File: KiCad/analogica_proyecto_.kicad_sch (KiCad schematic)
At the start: 0 parts

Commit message: afegit part analogica
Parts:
- added C1, C2: 1n, symbol Device:C
- added M1, M2: Conn_01x02_Pin, symbol Connector:Conn_01x02_Pin
- added U1: L298N, Package_TO_SOT_THT:TO-220-15_P2.54x5.08mm_StaggerOdd_Lead4.58mm_Vertical, symbol Driver_Motor:L298N
- added U2, U3: ACS714xLCTR-50A, Package_SO:SOIC-8_3.9x4.9mm_P1.27mm, symbol Sensor_Current:ACS714xLCTR-50A
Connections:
- new net: C1.1, U2.6 (FILTER)
- new net: C2.1, U3.6 (FILTER)
- new net AVSS: U2.8 (VCC), U3.8 (VCC)
- new net GND: C1.2, C2.2, U1.1 (SENSE_A), U1.15 (SENSE_B), U1.8 (GND), U2.5 (GND), U3.5 (GND)
- new net INA1_M1: U1.5 (IN1)
- new net INA2_M1: U1.7 (IN2)
- new net INB1_M2: U1.10 (IN3)
- new net INB2_M2: U1.12 (IN4)
- new net M1_OUT1: U1.2 (OUT1), U2.1 (IP+), U2.2 (IP+)
- new net M1_OUT2: M1.2 (Pin_2), U1.3 (OUT2)
- new net M1_OUTSEN: M1.1 (Pin_1), U2.3 (IP-), U2.4 (IP-)
- new net M2_OUT1: U1.13 (OUT3), U3.1 (IP+), U3.2 (IP+)
- new net M2_OUT2: M2.2 (Pin_2), U1.14 (OUT4)
- new net M2_OUTSEN: M2.1 (Pin_1), U3.3 (IP-), U3.4 (IP-)
- new net PWM_M1: U1.6 (EnA), U2.7 (VIOUT)
- new net PWM_M2: U1.11 (EnB), U3.7 (VIOUT)
- new net Vbat: U1.4 (Vs)
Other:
- note added: "ETAPA ANÀLOGICA"
- note added: "PONT en H"
- note added: "Pins motor"
- note added: "Sensor"

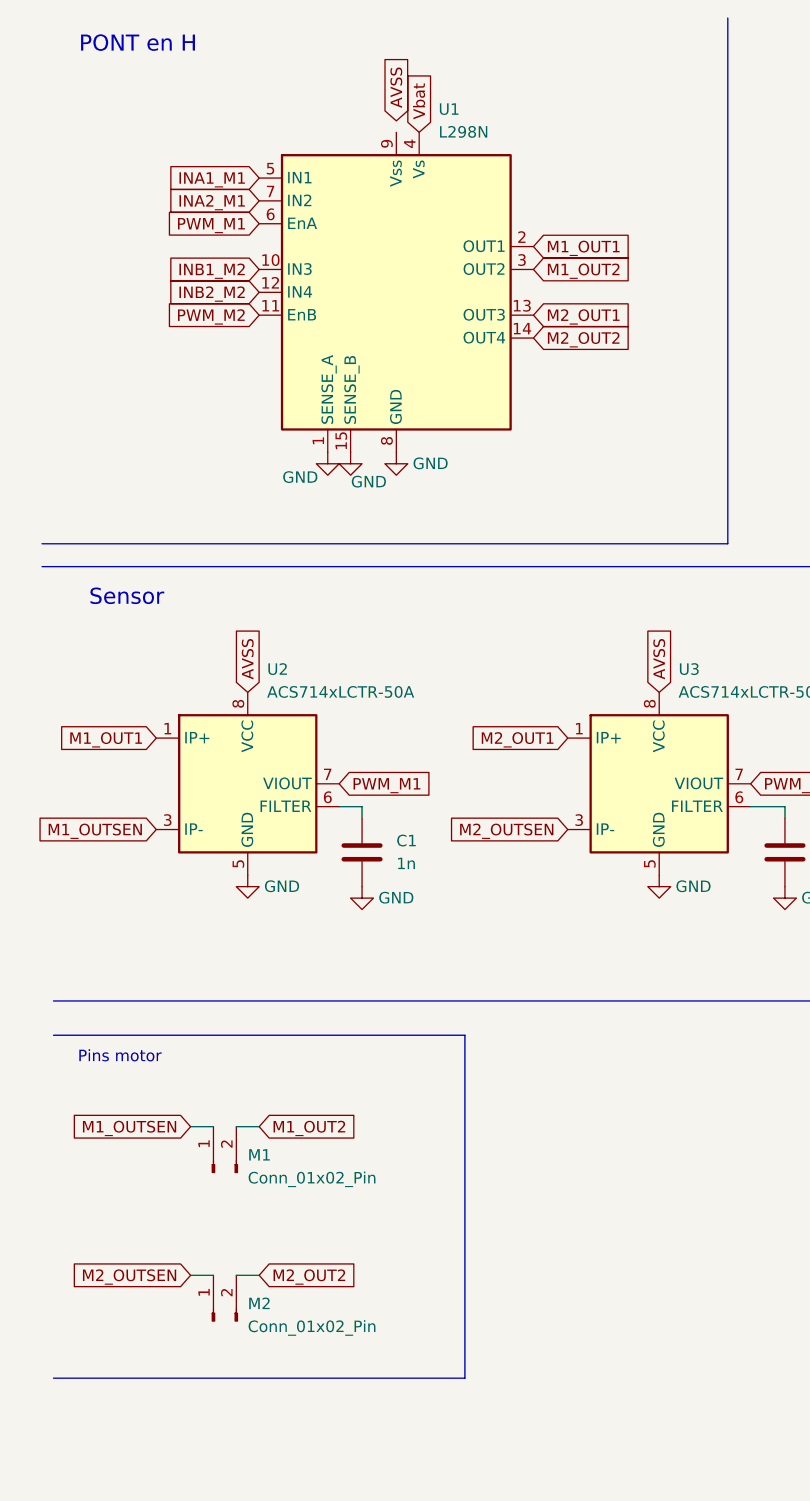
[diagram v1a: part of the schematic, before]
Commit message: Actualización ESquematico arreglandolo y corrigiendo fallos
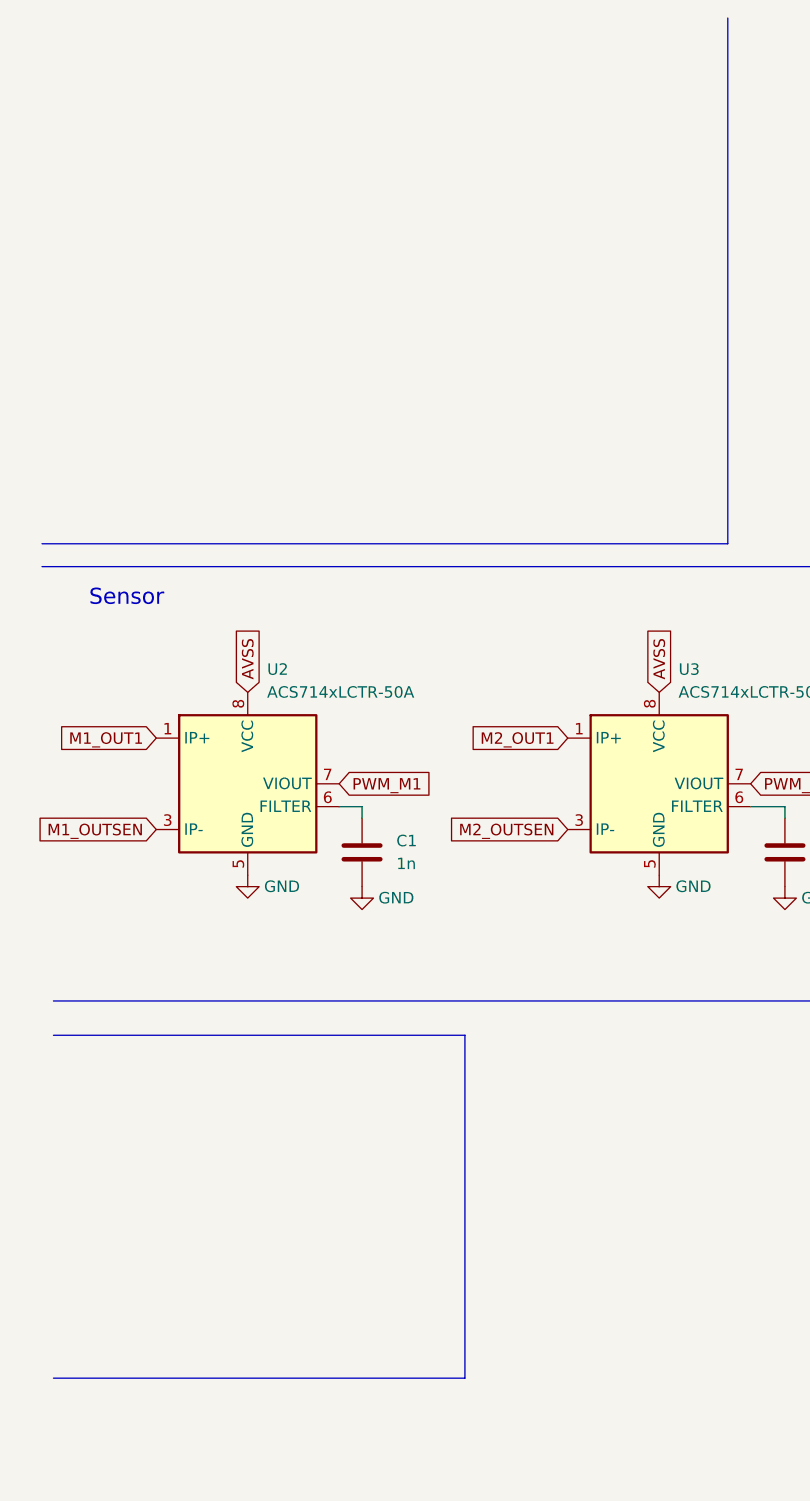
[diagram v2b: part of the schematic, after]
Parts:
- removed M1, M2: Conn_01x02_Pin, symbol Connector:Conn_01x02_Pin
- removed U1: L298N, Package_TO_SOT_THT:TO-220-15_P2.54x5.08mm_StaggerOdd_Lead4.58mm_Vertical, symbol Driver_Motor:L298N
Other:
- note removed: "PONT en H"
- note removed: "Pins motor"

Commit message: Nuevos cambios esquemativo v3
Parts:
- added C1, C2, C3, C4, C5, C6: 100n, symbol Device:C
- added R1, R10, R2, R9: 3.3k, symbol Device:R
- added R11, R12, R3, R4, R7, R8: 50, symbol Device:R
- added R5, R6: 3,3k, symbol Device:R
- added Rshunt1, Rshunt2: 0.05, symbol Device:R
- added U1, U2, U3: INA219AxD, Package_SO:SOIC-8_3.9x4.9mm_P1.27mm, symbol Sensor_Energy:INA219AxD
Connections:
- net GND: now also C1.2, C3.2, C5.2, R12.1, R4.1, Rshunt1.2, Rshunt2.2, U1.1 (A1), U1.2 (A0), U1.6 (GND), U2.1 (A1), U2.2 (A0), U2.6 (GND), U3.1 (A1), U3.6 (GND)
- new net +12V: R7.2
- new net AVDD: C1.1, C3.1, C5.1, R1.1, R10.1, R2.1, R5.1, R6.1, R9.1, U1.5 (VS), U2.5 (VS), U3.2 (A0), U3.5 (VS)
- new net I2C_SCL: R1.2, R5.2, R9.2, U1.4 (SCL), U2.4 (SCL), U3.4 (SCL)
- new net I2C_SDA: R10.2, R2.2, R6.2, U1.3 (SDA), U2.3 (SDA), U3.3 (SDA)
- new net IN+: C2.1, C4.1, C6.1, R11.1, R3.1, R7.1, U1.8 (IN+), U2.8 (IN+), U3.8 (IN+)
- new net IN-: C2.2, C4.2, C6.2, R12.2, R4.2, R8.2, U1.7 (IN-), U2.7 (IN-), U3.7 (IN-)
- new net SENSE_A: R3.2, Rshunt1.1
- new net SENSE_B: R11.2, Rshunt2.1
- new net Sensor_Atrapamiento_IN-: R8.1
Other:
- note added: "MOTOR 1 (cristal) A1: GND , A0: GND --> dirreción = 0 0 (para el I2C)"
- note added: "MOTOR 2 (cortineta) A1: GND , A0: VCC --> dirreción = 0 1 (para el I2C)"
- note added: "Sensor Anti-Atrapaments"
- note added: "Teniendo estas diferenes dirreciónes, podemos usar el mismo bus de I2C sabiendo bien de donde viene la señal (de que sensor viene) y así optimizando pines del microcontrolador."
- note removed: "Sensor"
- moved on the sheet: C1, C2, U2, U3

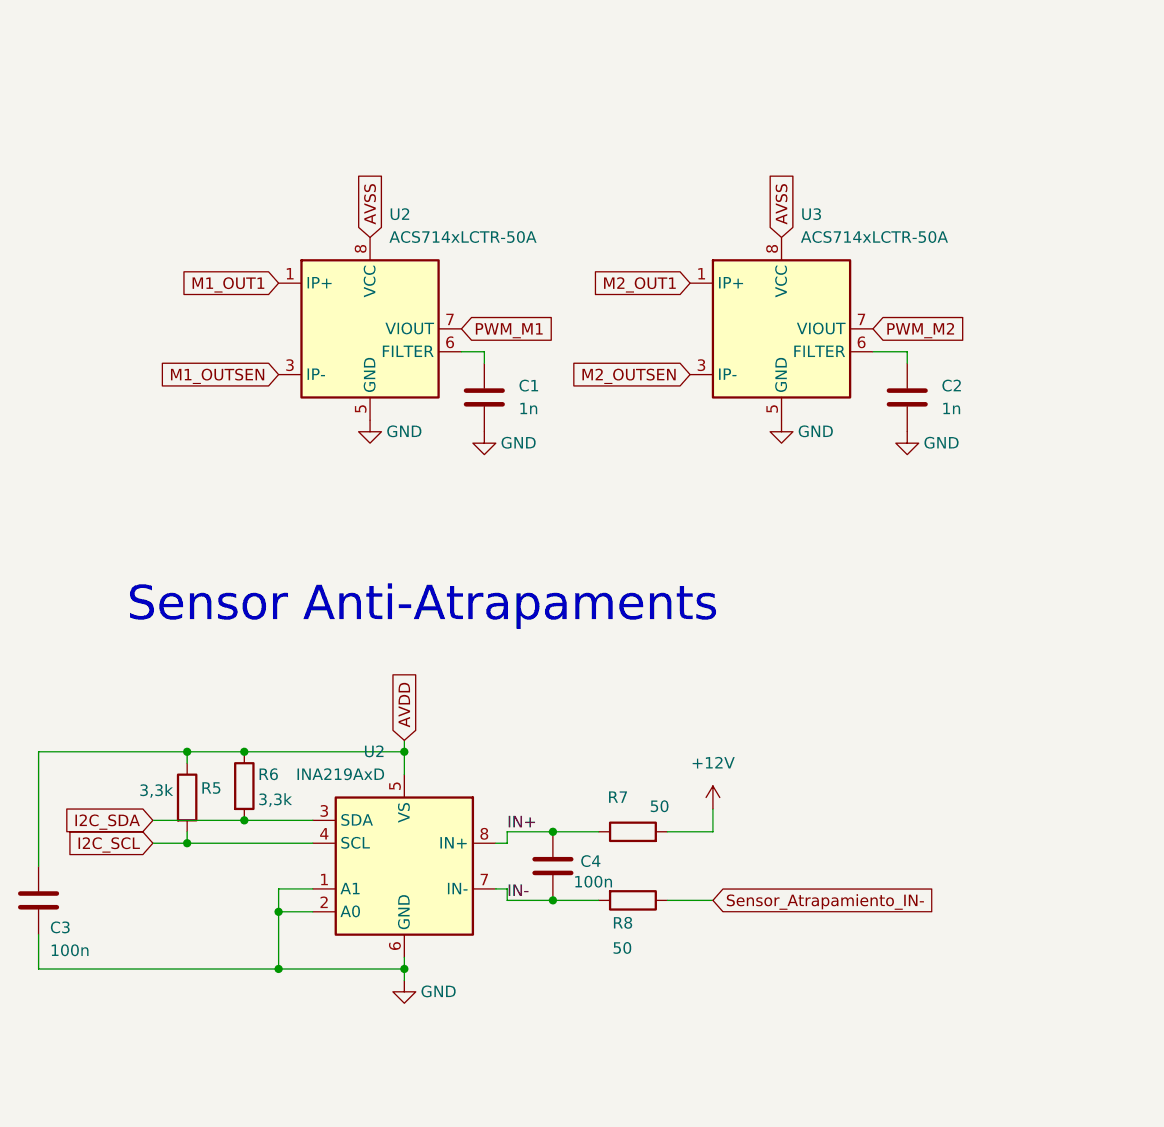
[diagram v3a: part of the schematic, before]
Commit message: Actualización de Esquematico, he puesto footprints y readme cambiado
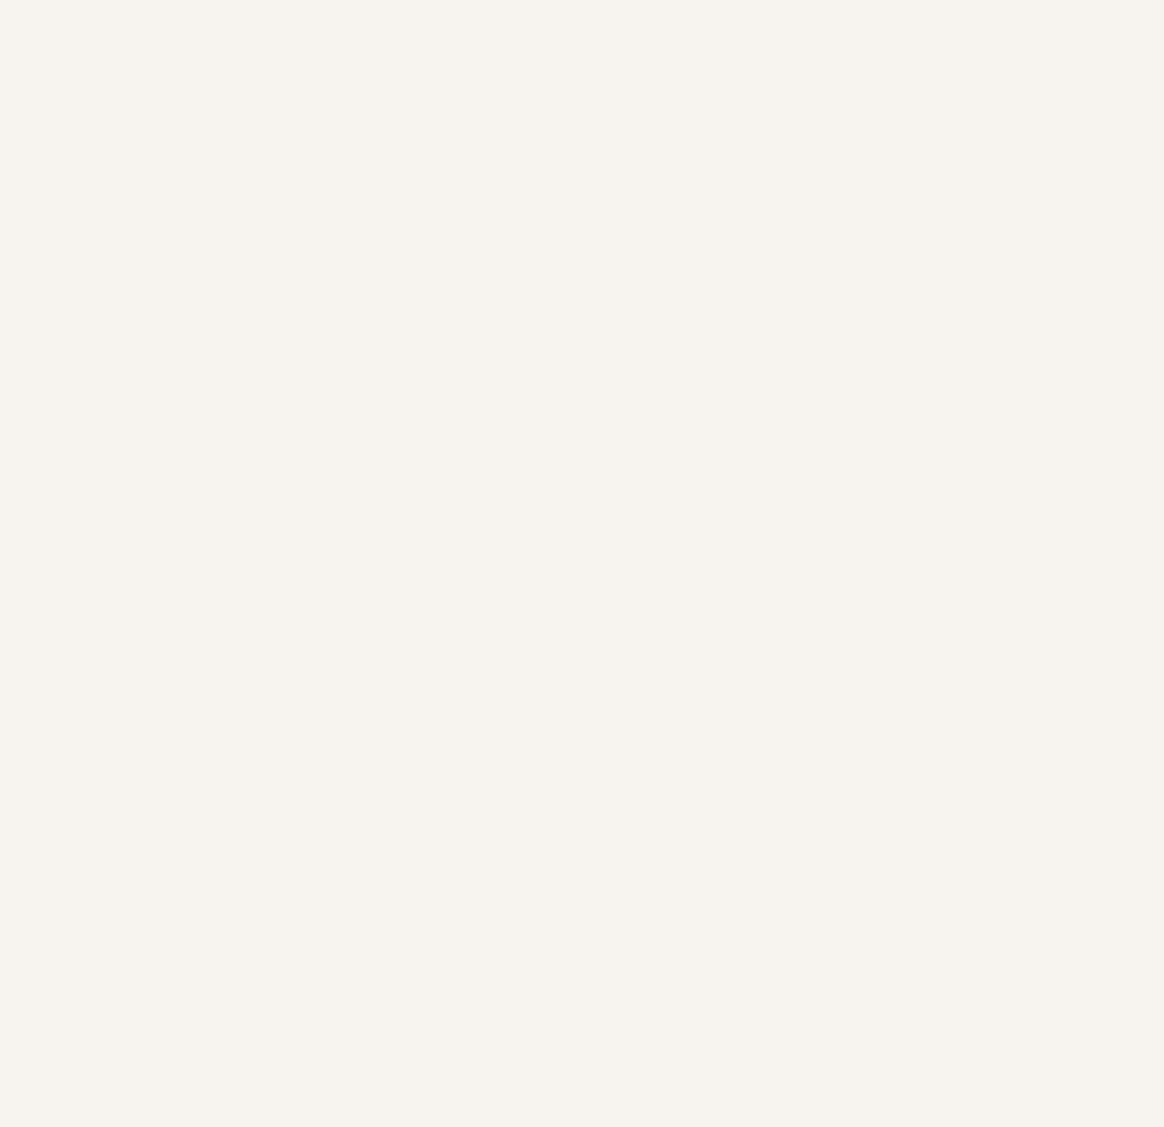
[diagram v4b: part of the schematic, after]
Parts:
- removed C1, C2: 1n, symbol Device:C
- removed C3, C4: 100n, symbol Device:C
- removed R5, R6: 3,3k, symbol Device:R
- removed R7, R8: 50, symbol Device:R
- removed U2: INA219AxD, Package_SO:SOIC-8_3.9x4.9mm_P1.27mm, symbol Sensor_Energy:INA219AxD
- removed U2, U3: ACS714xLCTR-50A, Package_SO:SOIC-8_3.9x4.9mm_P1.27mm, symbol Sensor_Current:ACS714xLCTR-50A
- C1, C2, C5, C6: footprint (none) -> Capacitor_SMD:C_0805_2012Metric
- R1, R10, R11, R12, R2, R3, R4, R9, Rshunt1, Rshunt2: footprint (none) -> Resistor_SMD:R_0805_2012Metric

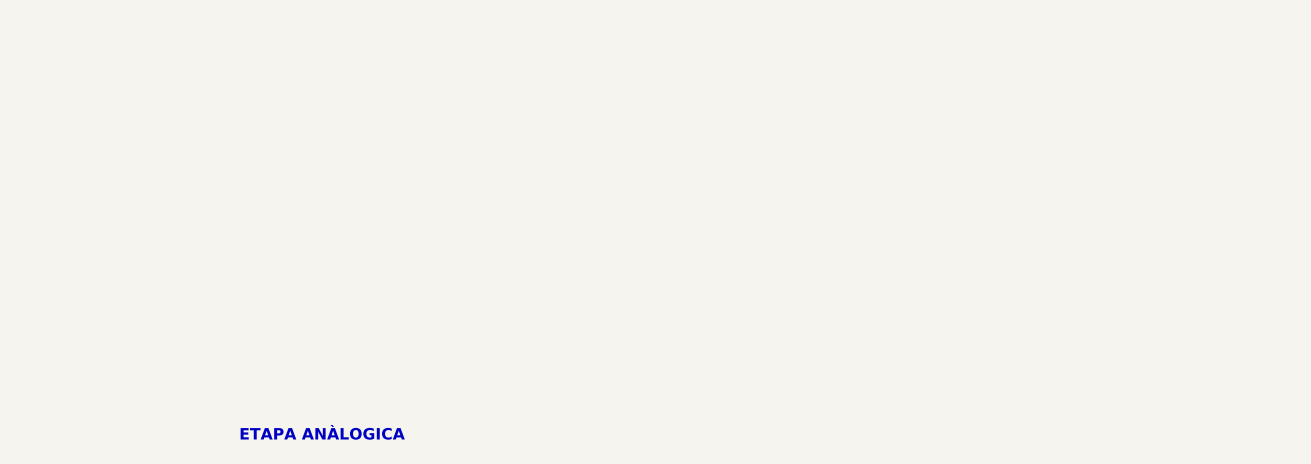
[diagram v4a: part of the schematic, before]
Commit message: Esquematico acabado y readme estructura base y componentes acabado y puesto el DB.
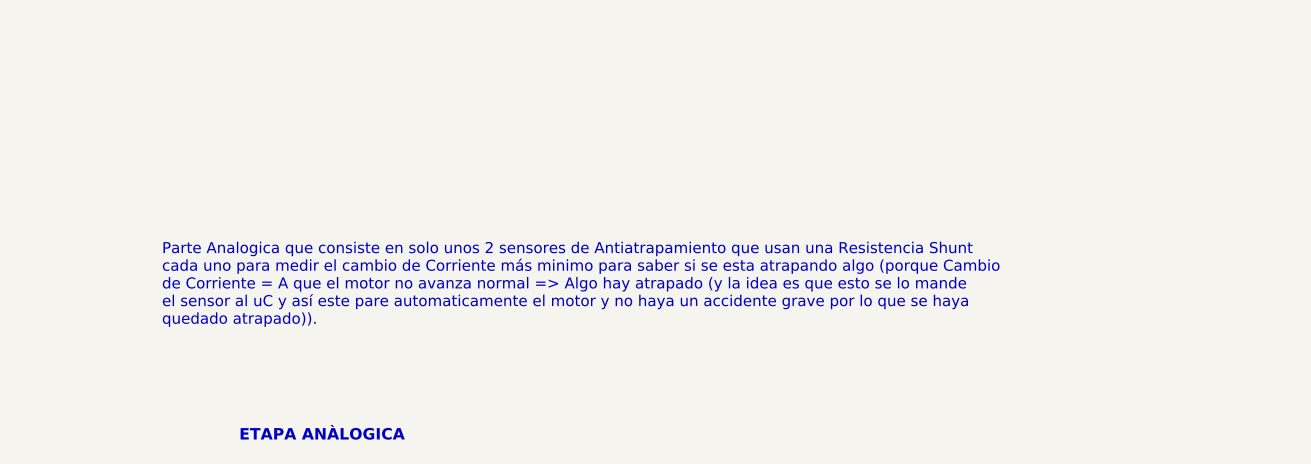
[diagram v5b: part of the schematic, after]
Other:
- note added: "Parte Analogica que consiste en solo unos 2 sensores de Antiatrapamiento que usan una Resistencia Shunt cada uno para medir el cambio de Corriente más minimo para saber si se esta atrapando algo (porque Cambio de Corriente = A que el motor no avanza normal => Algo hay atrapado (y la idea es que esto se lo mande el sensor al uC y así este pare automaticamente el motor y no haya un accidente grave 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"
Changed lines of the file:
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@@
+		)
+	)
+	(text "Parte Analogica que consiste en solo unos 2 sensores de Antiatrapamiento que usan una Resistencia Shunt \ncada uno para medir el cambio de Corriente más minimo para saber si se esta atrapando algo (porque Cambio\nde Corriente = A que el motor no avanza normal => Algo hay atrapado (y la idea es que esto se lo mande \nel sensor al uC y así este pare automaticamente el motor y no haya un accidente grave por lo que se haya \nquedado atrapado))."
+		(exclude_from_sim no)
+		(at 178.308 172.974 0)
+		(effects
+			(font
+				(size 1.2192 1.2192)
+			)
+			(justify left)
 		)
 	)

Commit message: Cambios al esquematico por SEsión 3
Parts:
- removed R10, R9: 3.3k, Resistor_SMD:R_0805_2012Metric, symbol Device:R
- renumbered C1 to C19, C5 to C20, C2 to C21, C6 to C22, R1 to R13, R2 to R15, R3 to R17, R4 to R18, R11 to R19, R12 to R20, U1 to U8, U3 to U9

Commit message: pujo el esquematico a medio hacer despues de hacer cambios para mejorar el 2o layout
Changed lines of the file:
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@@
 		(lib_id "Device:C")
 		(at 109.22 124.46 0)
+		(mirror y)
 		(unit 1)
 		(exclude_from_sim no)
@@
 		(dnp no)
 		(property "Reference" "C20"
-			(at 110.49 127.508 0)
+			(at 107.95 127.508 0)
 			(effects
 				(font
@@
 		)
 		(property "Value" "100n"
-			(at 110.49 130.048 0)
+			(at 107.95 130.048 0)
 			(effects
 				(font
@@
 		)
 		(property "Footprint" "Capacitor_SMD:C_0805_2012Metric"
-			(at 110.1852 128.27 0)
+			(at 108.2548 128.27 0)
 			(effects
 				(font

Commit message: Test Points y Parte POwer ruteada de nuevo
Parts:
- added TP_3V3, TP_5V, TP_GND1, TP_GND2, TP_GND3, TP_GNDPWM1, TP_GNDPWM2, TP_GNDPWM3, TP_GNDPWM4, TP_Vbat: TestPoint, symbol Connector:TestPoint
- added TP_PWM_M1, TP_PWM_M2, TP_Rshunt1, TP_Rshunt2, TP_SCL, TP_SDA: TestPoint_2Pole, symbol Connector:TestPoint_2Pole
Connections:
- net GND: now also TP_GND1.1, TP_GND2.1, TP_GND3.1, TP_PWM_M1.2, TP_PWM_M2.2, TP_SCL.2, TP_SDA.2; no longer R18.1, R20.1, Rshunt1.2, Rshunt2.2
- net I2C_SCL: now also TP_SCL.1
- net I2C_SDA: now also TP_SDA.1
- net SENSE_A: now also TP_Rshunt1.1
- net SENSE_B: now also TP_Rshunt2.1
- new net +3.3V: TP_3V3.1
- new net 5V: TP_5V.1
- new net GNDPWR: R18.1, R20.1, Rshunt1.2, Rshunt2.2, TP_GNDPWM1.1, TP_GNDPWM2.1, TP_GNDPWM3.1, TP_GNDPWM4.1, TP_Rshunt1.2, TP_Rshunt2.2
- new net INA1_M1: TP_PWM_M1.1
- new net INB2_M2: TP_PWM_M2.1
- new net Vbat: TP_Vbat.1
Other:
- note added: "ACORDARME DE PONER GNDPWM hasta el SEnsor Anti atrapamiento (GND de shunt) Y ACORDARSE DE QUE LAS LINEAS DE IN+ Y IN- DEL SENSOR DE ANTIATRAPAMIENTO DEBERIAN SER COMO EN EL CRISTAL, LO MENOS LARGAS POSIBLES Y SIMETRICAS UNA ENTRE LA OTRA"
- note added: "CERCA DEL CONECTOR ENTRADA DE ALIMENTACIÓN (VBAT)"
- note added: "CERCA DEL H_BRIDGE"
- note added: "CERCA DEL MICRO"
- note added: "CERCA DEL REGULADOR (LDO)"
- note added: "PWM de M1"
- note added: "PWM de M2"
- note added: "TEST POINTS"
- moved on the sheet: C19, C20, C21, C22, R13, R15, R17, R18, R19, R20, Rshunt1, Rshunt2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
